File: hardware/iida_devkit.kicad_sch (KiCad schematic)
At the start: 7 parts

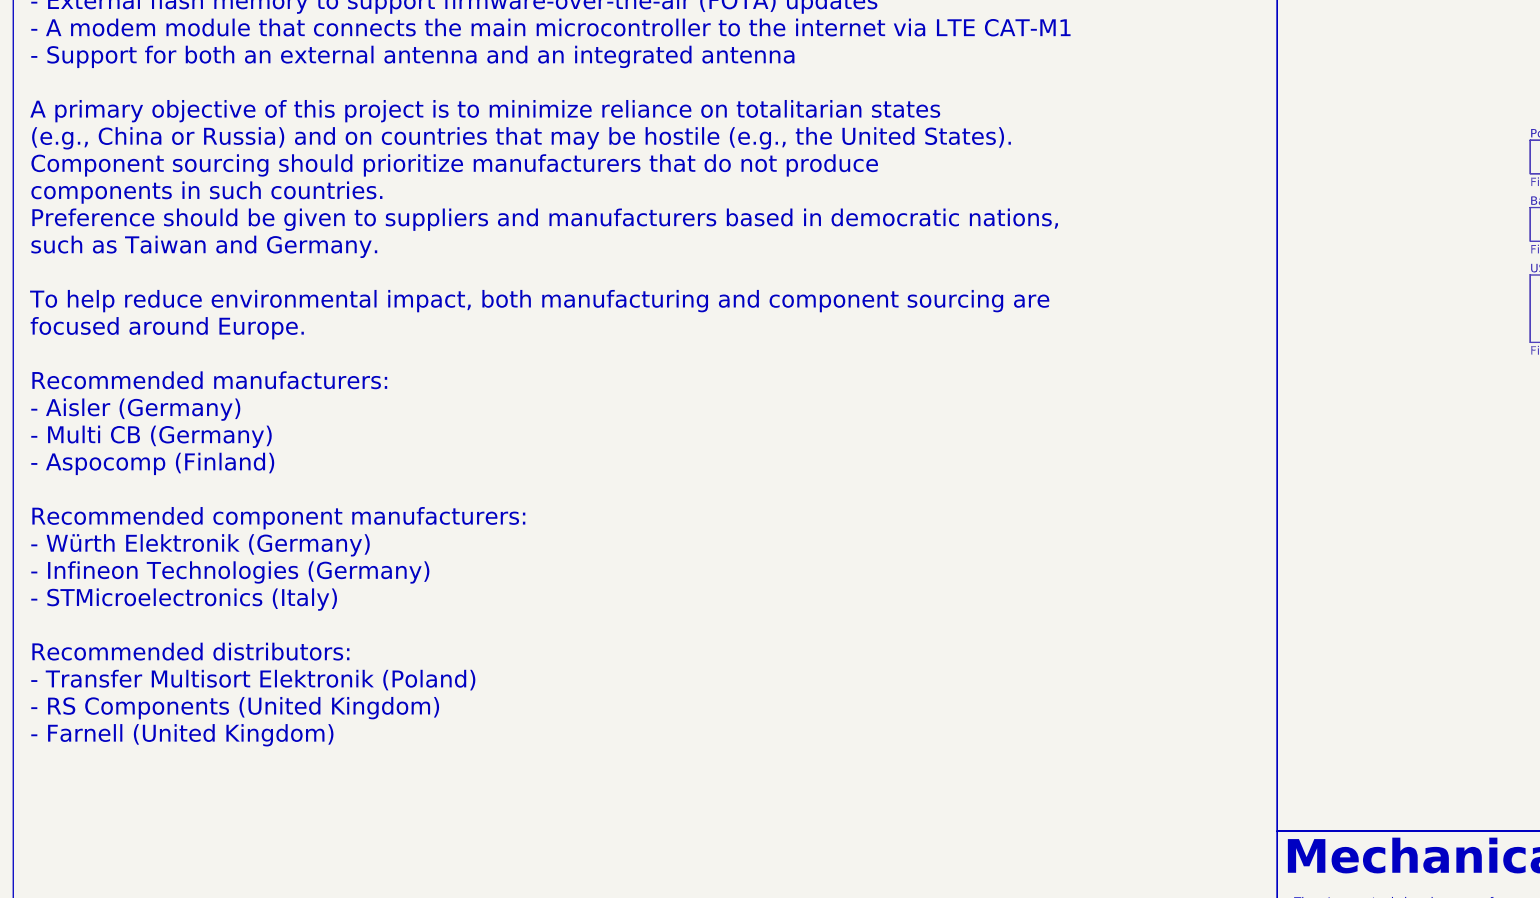
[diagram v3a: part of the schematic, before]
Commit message: HW: Explain component choices for power regulator
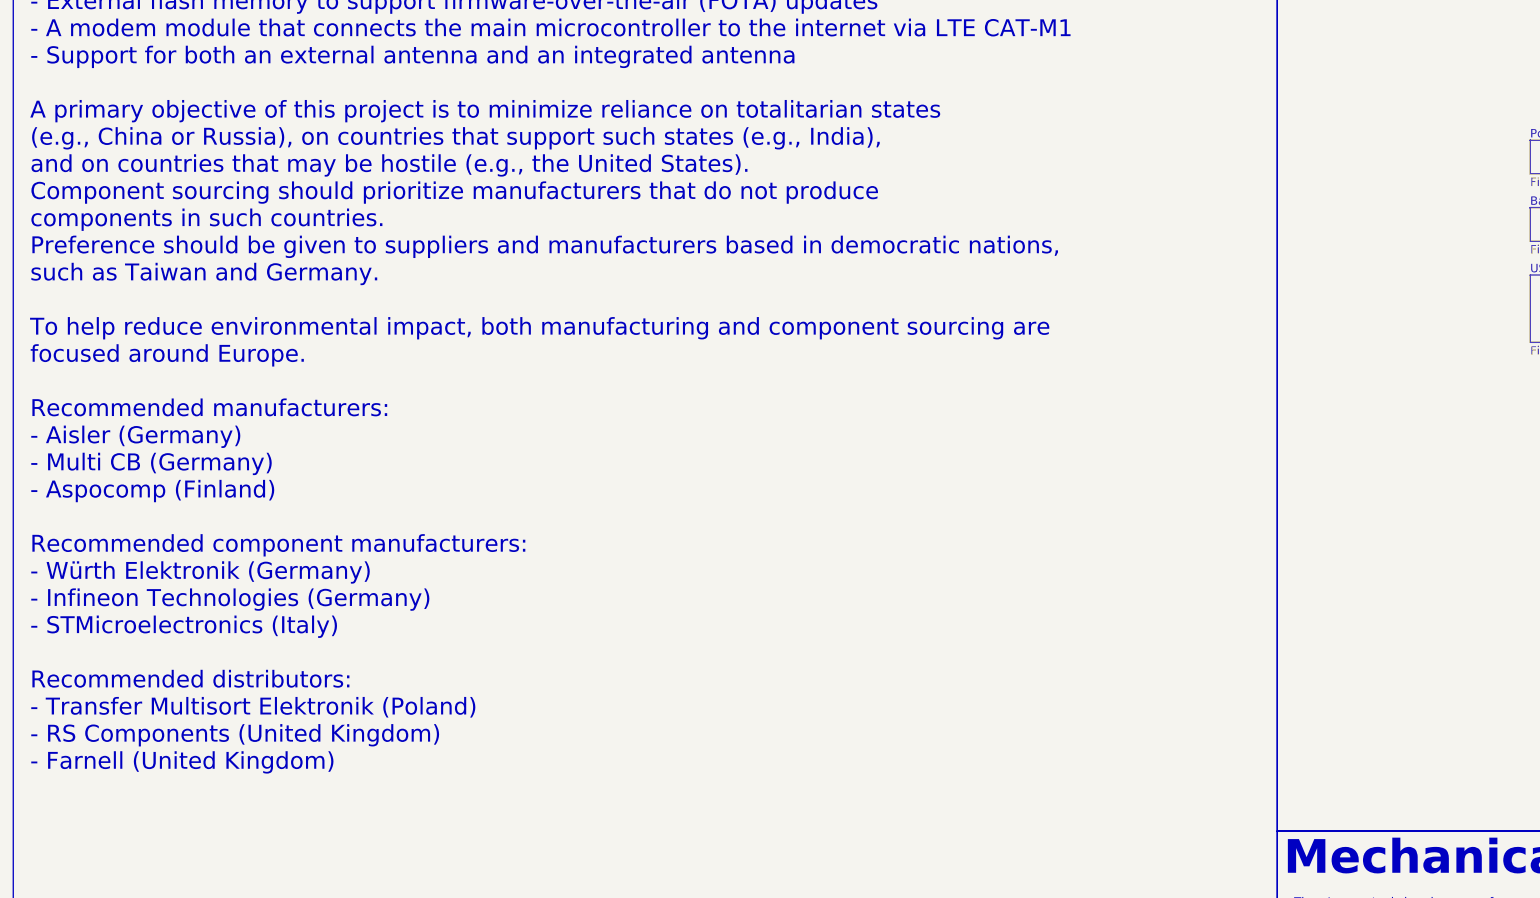
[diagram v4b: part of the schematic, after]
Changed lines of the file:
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@@
 	(title_block
 		(title "Iida devkit")
-		(date "2025-05-10")
+		(date "2025-05-12")
 		(rev "v5.0.0")
 	)
@@
 		)
 	)
-	(text "This project serves as a practice exercise in PCB design and embedded programming.\n\nThe result is a device that can be powered either by a battery or via a USB connection.\nThe device is capable of recharging the battery through the USB interface.\n\nKey features of the device include:\n- A sample sensor (temperature)\n- External flash memory to support firmware-over-the-air (FOTA) updates\n- A modem module that connects the main microcontroller to the internet via LTE CAT-M1\n- Support for both an external antenna and an integrated antenna\n\nA primary objective of this project is to minimize reliance on totalitarian states\n(e.g., China or Russia) and on countries that may be hostile (e.g., the United States).\nComponent sourcing should prioritize manufacturers that do not produce\ncomponents in such countries.\nPreference should be given to suppliers and manufacturers based in democratic nations,\nsuch as Taiwan and Germany.\n\nTo help reduce environmental impact, both manufacturing and component sourcing are\nfocused around Europe.\n\nRecommended manufacturers:\n- Aisler (Germany)\n- Multi CB (Germany)\n- Aspocomp (Finland)\n\nRecommended component manufacturers:\n- Würth Elektronik (Germany)\n- Infineon Technologies (Germany)\n- STMicroelectronics (Italy)\n\nRecommended distributors:\n- Transfer Multisort Elektronik (Poland)\n- RS Components (United Kingdom)\n- Farnell (United Kingdom)"
+	(text "This project serves as a practice exercise in PCB design and embedded programming.\n\nThe result is a device that can be powered either by a battery or via a USB connection.\nThe device is capable of recharging the battery through the USB interface.\n\nKey features of the device include:\n- A sample sensor (temperature)\n- External flash memory to support firmware-over-the-air (FOTA) updates\n- A modem module that connects the main microcontroller to the internet via LTE CAT-M1\n- Support for both an external antenna and an integrated antenna\n\nA primary objective of this project is to minimize reliance on totalitarian states\n(e.g., China or Russia), on countries that support such states (e.g., India),\nand on countries that may be hostile (e.g., the United States).\nComponent sourcing should prioritize manufacturers that do not produce\ncomponents in such countries.\nPreference should be given to suppliers and manufacturers based in democratic nations,\nsuch as Taiwan and Germany.\n\nTo help reduce environmental impact, both manufacturing and component sourcing are\nfocused around Europe.\n\nRecommended manufacturers:\n- Aisler (Germany)\n- Multi CB (Germany)\n- Aspocomp (Finland)\n\nRecommended component manufacturers:\n- Würth Elektronik (Germany)\n- Infineon Technologies (Germany)\n- STMicroelectronics (Italy)\n\nRecommended distributors:\n- Transfer Multisort Elektronik (Poland)\n- RS Components (United Kingdom)\n- Farnell (United Kingdom)"
 		(exclude_from_sim no)
 		(at 15.24 63.5 0)

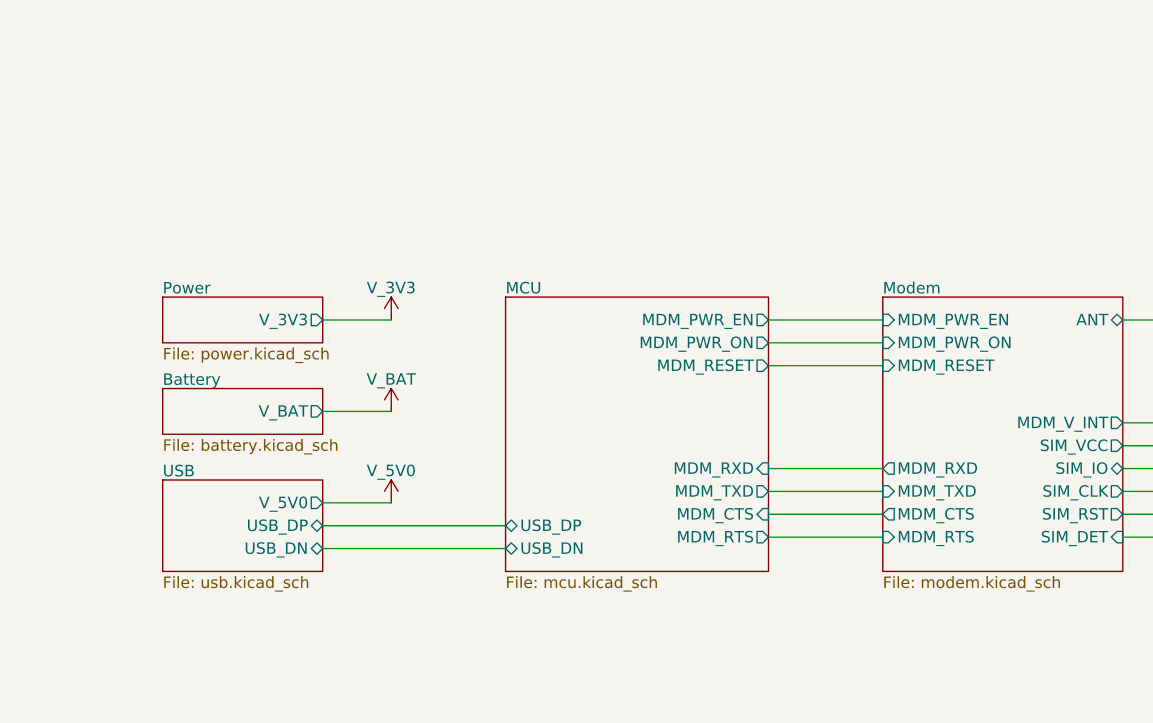
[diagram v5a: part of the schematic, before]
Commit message: HW: Add battery monitoring with MAX17048
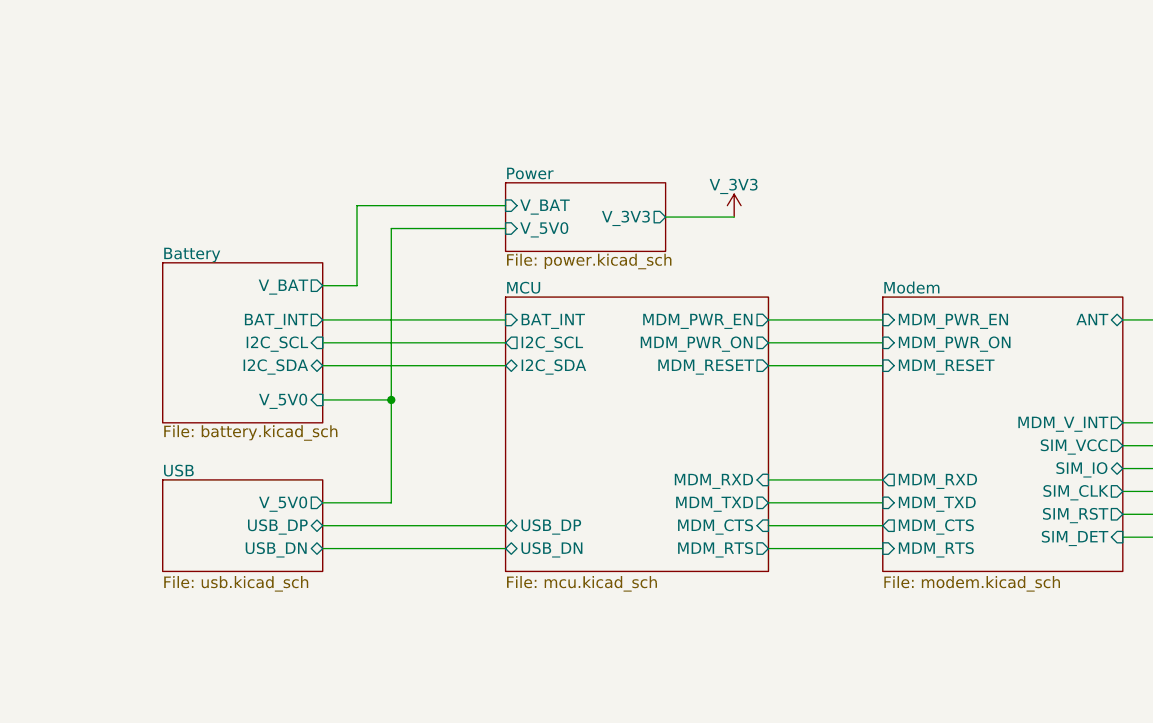
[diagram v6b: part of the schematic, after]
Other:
- sheet Battery ports: added BAT_INT, I2C_SCL, I2C_SDA, V_5V0; removed none
- sheet MCU ports: added BAT_INT, I2C_SCL, I2C_SDA; removed none
- sheet Power ports: added V_5V0, V_BAT; removed none

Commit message: HW: Reorganize schematic
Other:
- added sheet IO expander (io_expander.kicad_sch)
- added sheet Sensors (sensors.kicad_sch)
- sheet Battery ports: added BAT_INTn; removed BAT_INT
- sheet MCU ports: added IO_EXP_INT; removed BAT_INT, MDM_PWR_EN, MDM_PWR_ON, MDM_RESET
